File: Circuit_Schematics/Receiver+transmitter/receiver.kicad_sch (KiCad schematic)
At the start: 17 parts, among them SW1 SW_Push, SW2 SW_Push, SW3 SW_Push, SW4 SW_Push, SW5 SW_Push, U4 RASPBERRY_PI_PICO, U5 LCD Display, U6 Micro SD holder, U7 RF Transmitter

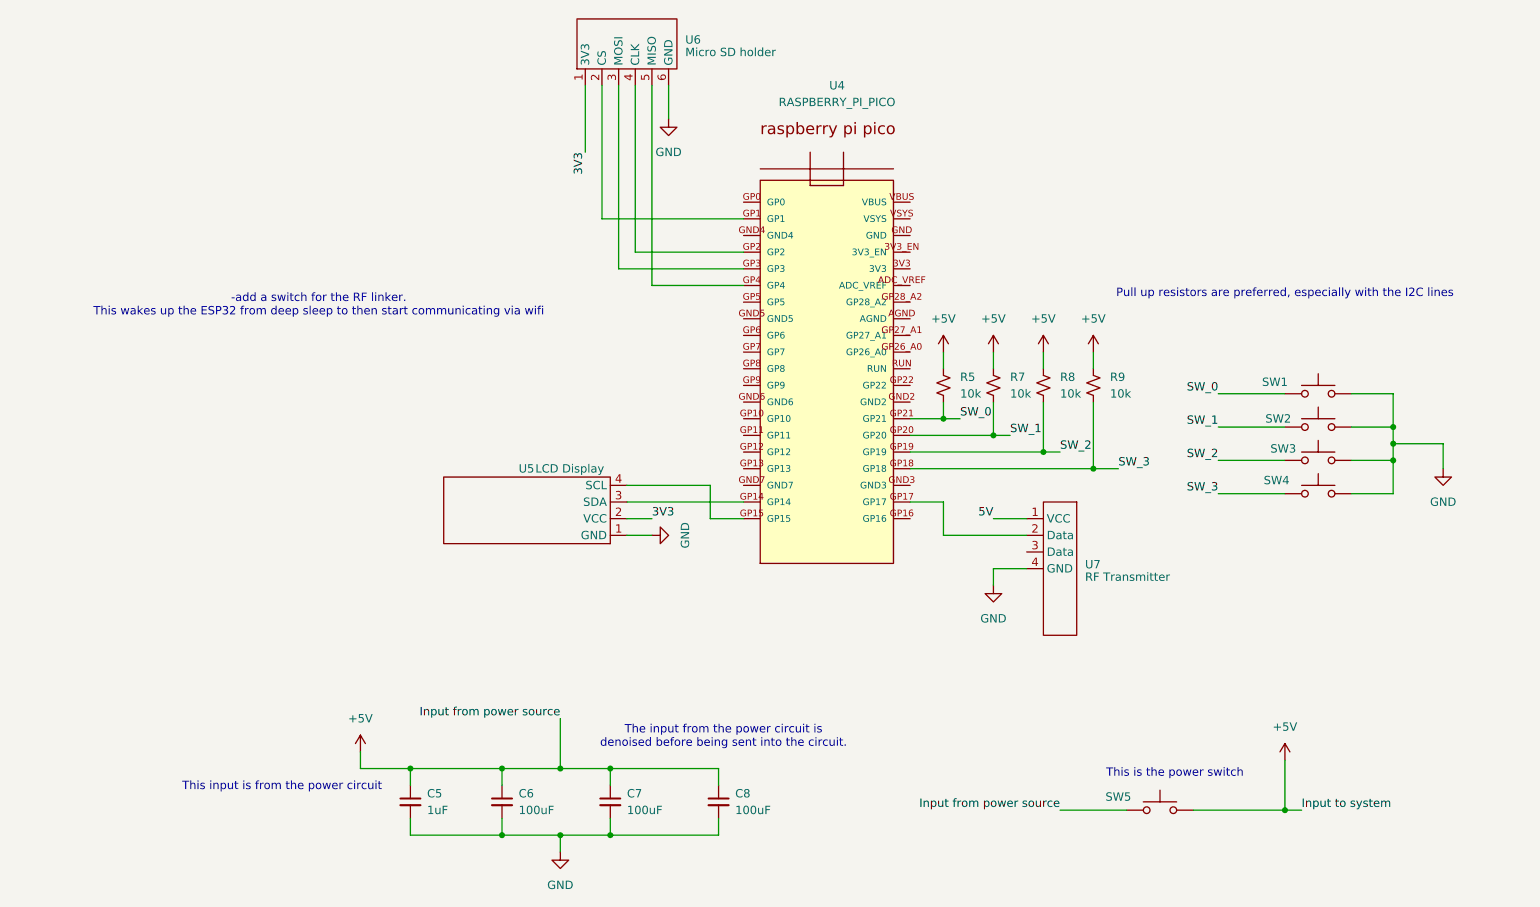
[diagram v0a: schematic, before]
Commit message: Final revision of KiCAD Docs
Edited the transmitter and receiver schematics to reflect the recent changes
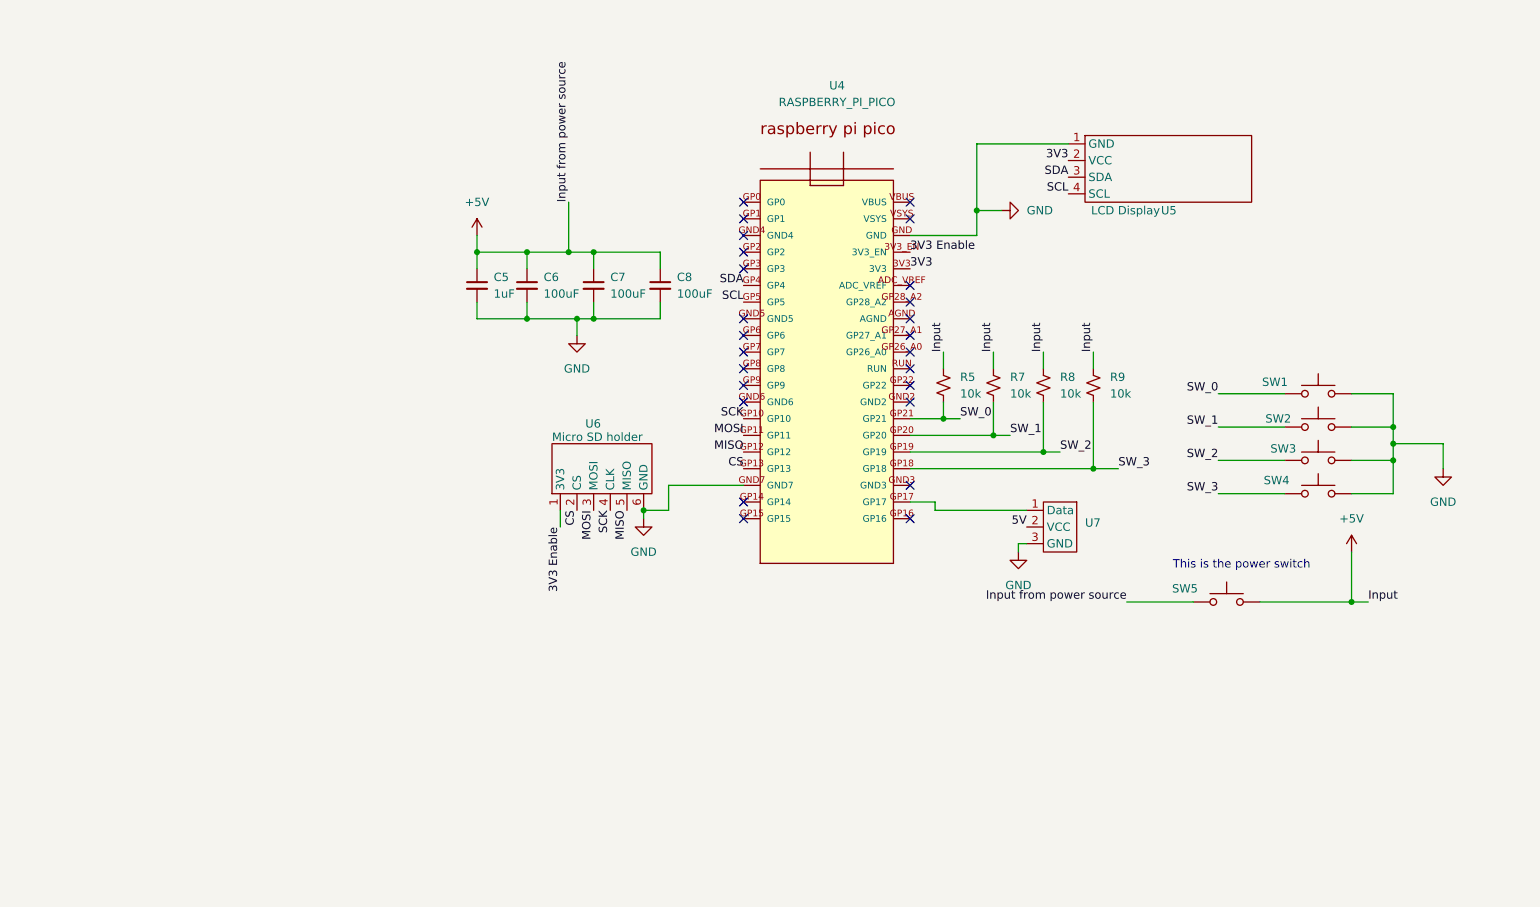
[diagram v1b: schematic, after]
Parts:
- removed U7: RF Transmitter, symbol Component:RF_Linker_Transmitter
- added U7: ~, symbol Component:RF_Transmitter
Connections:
- net 3V3: now also U4.3V3; no longer U6.1 (3V3)
- net 5V: now also U7.2 (VCC)
- net GND: now also U4.GND, U4.GND7, U7.3 (GND)
- net at U4.GP1: no longer U6.2 (CS)
- net at U4.GP3: no longer U6.3 (MOSI)
- net at U4.GP2: no longer U6.4 (CLK)
- net MISO: now reaches U6.5 (MISO)
- net MISO: now also U4.GP12; no longer U4.GP4
- net at U4.GP14: no longer U5.3 (SDA)
- net at U4.GP15: no longer U5.4 (SCL)
- net at U4.GP17: now also U7.1 (Data)
- net 3V3 Enable: now reaches U4.3V3_EN
- net 3V3 Enable: now also U6.1 (3V3)
- net SCK: now reaches U4.GP10
- net SCK: now also U6.4 (CLK)
- net MOSI: now reaches U4.GP11
- net MOSI: now also U6.3 (MOSI)
- net CS: now reaches U4.GP13
- net CS: now also U6.2 (CS)
- net SCL: now reaches U4.GP5
- net SCL: now also U5.4 (SCL)
- new net SDA: U4.GP4, U5.3 (SDA)
- no-connect marks 0 -> 25
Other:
- note removed: "-add a switch for the RF linker. This wakes up the ESP32 from deep sleep to then start communicating via wifi"
- note removed: "Pull up resistors are preferred, especially with the I2C lines"
- note removed: "The input from the power circuit is denoised before being sent into the circuit."
- note removed: "This input is from the power circuit"
- moved on the sheet: C5, C6, C7, C8, SW5, U5, U6
